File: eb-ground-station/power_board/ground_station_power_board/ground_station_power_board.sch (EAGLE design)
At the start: 70 parts, among them J1 CONN_20X2SHROUDED, Q1 SQJ459EP_MOSFET_P_CHAN, Q15 DMN61D8LVT-DUAL-N-CHANNEL-MOS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, Q17 DMN61D8LVT-DUAL-N-CHANNEL-MOS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, Q18 DMN61D8LVT-DUAL-N-CHANNEL-MOS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, Q2 SQJ459EP_MOSFET_P_CHAN, Q22 TC4427-FET-GATE-DRVR, Q23 TC4427-FET-GATE-DRVR, Q24 TC4427-FET-GATE-DRVR, Q3 SQJ459EP_MOSFET_P_CHAN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

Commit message: every time I look at this I add 40 more vias
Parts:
- added J2: (no value), SparkFun-Connectors:CONN_01PTH_NO_SILK_KIT
- added R14: 4.7k, SparkFun-Resistors:4.7KOHM-0603-1/10W-1%
- R10, R8, R9: value EXB-A10P391JC_ARRAY_EXBA-M -> 10k
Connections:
- new net N$6: J2.1, R14.1, U2.!RESET
- net 3.3V: now also R14.2
- net GND: no longer U2.!RESET
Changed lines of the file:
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@@
 <?xml version="1.0" encoding="utf-8"?>
 <!DOCTYPE eagle SYSTEM "eagle.dtd">
-<eagle version="9.1.0">
+<eagle version="9.1.1">
 <drawing>
 <settings>
@@
 <layer number="90" name="Modules" color="5" fill="1" visible="no" active="yes"/>
 <layer number="91" name="Nets" color="2" fill="1" visible="yes" active="yes"/>
-<layer number="92" name="Busses" color="1" fill="1" visible="no" active="yes"/>
+<layer number="92" name="Busses" color="1" fill="1" visible="yes" active="yes"/>
 <layer number="93" name="Pins" color="2" fill="1" visible="no" active="yes"/>
 <layer number="94" name="Symbols" color="4" fill="1" visible="yes" active="yes"/>
@@
 <part name="U1" library="GROUND-STATION-POWER-BOARD" deviceset="ADS1115IDGST" device="DGS10-M"/>
 <part name="U2" library="GROUND-STATION-POWER-BOARD" deviceset="MCP23017T-E/SO" device="QFN" value="MCP23017T-E/SOQFN"/>
-<part name="R9" library="temp-lib" deviceset="EXB-A10P391J" device="C_ARRAY_EXBA-M"/>
-<part name="R8" library="temp-lib" deviceset="EXB-A10P391J" device="C_ARRAY_EXBA-M"/>
+<part name="R9" library="temp-lib" deviceset="EXB-A10P391J" device="C_ARRAY_EXBA-M" value="10k"/>
+<part name="R8" library="temp-lib" deviceset="EXB-A10P391J" device="C_ARRAY_EXBA-M" value="10k"/>
 <part name="GND1" library="SparkFun-PowerSymbols" deviceset="GND" device=""/>
 <part name="GND2" library="SparkFun-PowerSymbols" deviceset="GND" device=""/>
@@
 <part name="R2" library="SparkFun-Resistors" deviceset="4.7KOHM" device="-0603-1/10W-1%" value="4.7k"/>
 <part name="SUPPLY20" library="SparkFun-PowerSymbols" deviceset="3.3V" device=""/>
-<part name="R10" library="temp-lib" deviceset="EXB-A10P391J" device="C_ARRAY_EXBA-M"/>
+<part name="R10" library="temp-lib" deviceset="EXB-A10P391J" device="C_ARRAY_EXBA-M" value="10k"/>
 <part name="SUPPLY21" library="SparkFun-PowerSymbols" deviceset="12V" device=""/>
 <part name="R12" library="GROUND-STATION-POWER-BOARD" deviceset="RES-ARRAY-742C083" device="" value="220"/>
@@
 <part name="Q6" library="GROUND-STATION-POWER-BOARD" deviceset="SQJ459EP_MOSFET_P_CHAN" device=""/>
 <part name="FRAME1" library="frames" library_urn="urn:adsk.eagle:library:229" deviceset="FRAME_B_L" device=""/>
+<part name="R14" library="SparkFun-Resistors" deviceset="4.7KOHM" device="-0603-1/10W-1%" value="4.7k"/>
+<part name="SUPPLY15" library="SparkFun-PowerSymbols" deviceset="3.3V" device=""/>
+<part name="J2" library="SparkFun-Connectors" deviceset="CONN_01" device="PTH_NO_SILK_KIT"/>
 </parts>
 <sheets>
@@
 <attribute name="VALUE" x="-66.3194" y="489.1786" size="1.27" layer="96" ratio="6" rot="SR0"/>
 </instance>
-<instance part="R9" gate="A" x="21.59" y="482.6" smashed="yes"/>
+<instance part="R9" gate="A" x="21.59" y="482.6" smashed="yes">
+<attribute name="VALUE" x="22.7076" y="474.5228" size="1.27" layer="96" ratio="10" rot="SR0"/>
+<attribute name="NAME" x="22.5552" y="476.5548" size="1.27" layer="95" ratio="10" rot="SR0"/>
+</instance>
 <instance part="R8" gate="A" x="21.59" y="462.28" smashed="yes">
-<attribute name="NAME" x="1.9812" y="470.7128" size="1.27" layer="95" ratio="10" rot="SR0"/>
+<attribute name="VALUE" x="22.4536" y="455.7268" size="1.27" layer="96" ratio="10" rot="SR0"/>
+<attribute name="NAME" x="22.3012" y="458.0128" size="1.27" layer="95" ratio="10" rot="SR0"/>
 </instance>
 <instance part="GND1" gate="1" x="26.67" y="467.36" smashed="yes">
@@
 <attribute name="VALUE" x="-39.37" y="336.804" size="1.27" layer="96" align="bottom-center"/>
 </instance>
-<instance part="GND7" gate="1" x="-73.66" y="447.04" smashed="yes">
-<attribute name="VALUE" x="-73.66" y="446.786" size="1.27" layer="96" align="top-center"/>
+<instance part="GND7" gate="1" x="-78.74" y="459.74" smashed="yes">
+<attribute name="VALUE" x="-78.74" y="459.486" size="1.27" layer="96" align="top-center"/>
 </instance>
 <instance part="GND8" gate="1" x="-50.8" y="424.18" smashed="yes">
@@
 </instance>
 <instance part="R10" gate="A" x="170.18" y="383.54" smashed="yes">
-<attribute name="NAME" x="172.1612" y="369.1128" size="1.27" layer="95" ratio="10" rot="SR0"/>
+<attribute name="VALUE" x="171.0436" y="369.8748" size="1.27" layer="96" ratio="10" rot="SR0"/>
+<attribute name="NAME" x="170.8912" y="371.6528" size="1.27" layer="95" ratio="10" rot="SR0"/>
 </instance>
 <instance part="SUPPLY21" gate="G$1" x="175.26" y="375.92" smashed="yes">
@@
 <instance part="FRAME1" gate="G$1" x="-93.98" y="231.14"/>
 <instance part="FRAME1" gate="G$2" x="231.14" y="231.14"/>
+<instance part="R14" gate="G$1" x="-83.82" y="457.2" smashed="yes" rot="R90">
+<attribute name="NAME" x="-85.344" y="457.2" size="1.27" layer="95" font="vector" rot="R90" align="bottom-center"/>
+<attribute name="VALUE" x="-82.296" y="457.2" size="1.27" layer="96" font="vector" rot="R90" align="top-center"/>
+</instance>
+<instance part="SUPPLY15" gate="G$1" x="-83.82" y="463.804" smashed="yes">
+<attribute name="VALUE" x="-83.82" y="466.598" size="1.27" layer="96" align="bottom-center"/>
+</instance>
+<instance part="J2" gate="G$1" x="-83.82" y="439.42" rot="R90"/>
 </instances>
 <busses>
@@
 <wire x1="26.67" y1="469.9" x2="26.67" y2="472.44" width="0.1524" layer="91"/>
 <wire x1="26.67" y1="472.44" x2="24.13" y2="472.44" width="0.1524" layer="91"/>
-</segment>
-<segment>
-<pinref part="GND7" gate="1" pin="GND"/>
-<pinref part="U2" gate="A" pin="!RESET"/>
-<wire x1="-73.66" y1="449.58" x2="-73.66" y2="452.12" width="0.1524" layer="91"/>
-<wire x1="-73.66" y1="452.12" x2="-71.12" y2="452.12" width="0.1524" layer="91"/>
-<pinref part="U2" gate="A" pin="A0"/>
-<wire x1="-71.12" y1="462.28" x2="-73.66" y2="462.28" width="0.1524" layer="91"/>
-<wire x1="-73.66" y1="462.28" x2="-73.66" y2="459.74" width="0.1524" layer="91"/>
-<junction x="-73.66" y="452.12"/>
-<pinref part="U2" gate="A" pin="A1"/>
-<wire x1="-73.66" y1="459.74" x2="-73.66" y2="457.2" width="0.1524" layer="91"/>
-<wire x1="-73.66" y1="457.2" x2="-73.66" y2="452.12" width="0.1524" layer="91"/>
-<wire x1="-71.12" y1="459.74" x2="-73.66" y2="459.74" width="0.1524" layer="91"/>
-<junction x="-73.66" y="459.74"/>
-<pinref part="U2" gate="A" pin="A2"/>
-<wire x1="-71.12" y1="457.2" x2="-73.66" y2="457.2" width="0.1524" layer="91"/>
-<junction x="-73.66" y="457.2"/>
 </segment>
 <segment>
@@
 <wire x1="-43.18" y1="297.18" x2="-43.18" y2="300.99" width="0.1524" layer="91"/>
 </segment>
+<segment>
+<pinref part="U2" gate="A" pin="A0"/>
+<wire x1="-71.12" y1="462.28" x2="-73.66" y2="462.28" width="0.1524" layer="91"/>
+<wire x1="-73.66" y1="462.28" x2="-73.66" y2="459.74" width="0.1524" layer="91"/>
+<pinref part="U2" gate="A" pin="A1"/>
+<wire x1="-73.66" y1="459.74" x2="-73.66" y2="457.2" width="0.1524" layer="91"/>
+<wire x1="-71.12" y1="459.74" x2="-73.66" y2="459.74" width="0.1524" layer="91"/>
+<junction x="-73.66" y="459.74"/>
+<pinref part="U2" gate="A" pin="A2"/>
+<wire x1="-71.12" y1="457.2" x2="-73.66" y2="457.2" width="0.1524" layer="91"/>
+<pinref part="GND7" gate="1" pin="GND"/>
+<wire x1="-78.74" y1="462.28" x2="-73.66" y2="462.28" width="0.1524" layer="91"/>
+<junction x="-73.66" y="462.28"/>
+</segment>
 </net>
 <net name="12V" class="0">
@@
 <pinref part="SUPPLY9" gate="G$1" pin="3.3V"/>
 <wire x1="-44.45" y1="334.01" x2="-39.37" y2="334.01" width="0.1524" layer="91"/>
+</segment>
+<segment>
+<pinref part="SUPPLY15" gate="G$1" pin="3.3V"/>
+<pinref part="R14" gate="G$1" pin="2"/>
+<wire x1="-83.82" y1="463.804" x2="-83.82" y2="462.28" width="0.1524" layer="91"/>
 </segment>
 </net>
@@
 </segment>
 </net>
+<net name="N$6" class="0">
+<segment>
+<pinref part="U2" gate="A" pin="!RESET"/>
+<pinref part="R14" gate="G$1" pin="1"/>
+<wire x1="-71.12" y1="452.12" x2="-83.82" y2="452.12" width="0.1524" layer="91"/>
+<pinref part="J2" gate="G$1" pin="1"/>
+<wire x1="-83.82" y1="452.12" x2="-83.82" y2="447.04" width="0.1524" layer="91"/>
+<junction x="-83.82" y="452.12"/>
+</segment>
+</net>

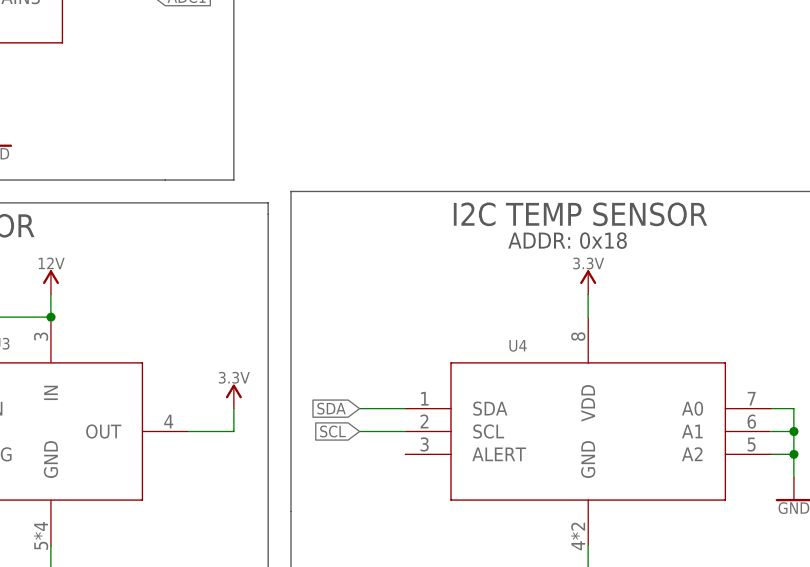
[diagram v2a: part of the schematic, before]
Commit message: added decoupling cap and some labels
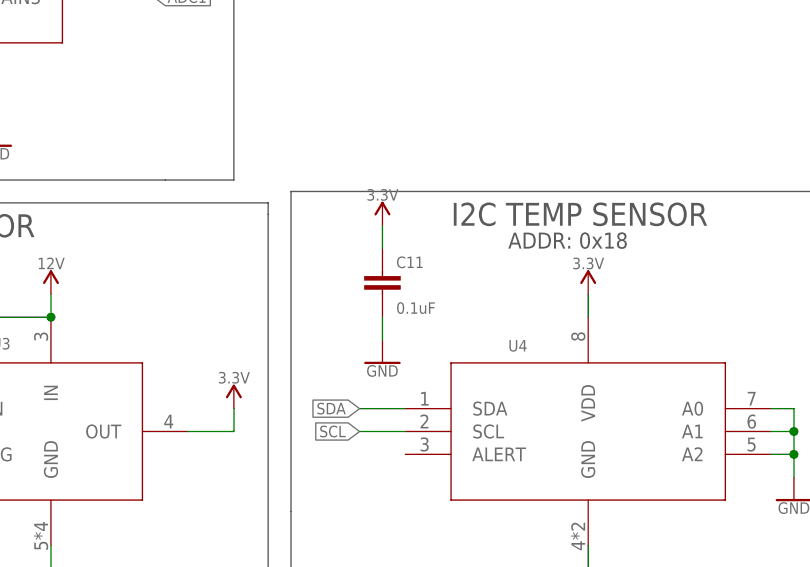
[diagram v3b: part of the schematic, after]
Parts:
- added C11: 0.1uF, SparkFun-Capacitors:0.1UF-0603-25V-5%
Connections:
- net 3.3V: now also C11.1
- net GND: now also C11.2
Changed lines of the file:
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@@
 <part name="SUPPLY15" library="SparkFun-PowerSymbols" deviceset="3.3V" device=""/>
 <part name="J2" library="SparkFun-Connectors" deviceset="CONN_01" device="PTH_NO_SILK_KIT"/>
+<part name="C11" library="SparkFun-Capacitors" deviceset="0.1UF" device="-0603-25V-5%" value="0.1uF"/>
+<part name="SUPPLY27" library="SparkFun-PowerSymbols" deviceset="3.3V" device=""/>
+<part name="GND3" library="SparkFun-PowerSymbols" deviceset="GND" device=""/>
 </parts>
 <sheets>
@@
 </instance>
 <instance part="J2" gate="G$1" x="-83.82" y="439.42" rot="R90"/>
+<instance part="C11" gate="G$1" x="0" y="278.13" smashed="yes">
+<attribute name="NAME" x="1.524" y="281.051" size="1.27" layer="95" font="vector"/>
+<attribute name="VALUE" x="1.524" y="275.971" size="1.27" layer="96" font="vector"/>
+</instance>
+<instance part="SUPPLY27" gate="G$1" x="0" y="285.75" smashed="yes">
+<attribute name="VALUE" x="0" y="288.544" size="1.27" layer="96" align="bottom-center"/>
+</instance>
+<instance part="GND3" gate="1" x="0" y="270.51" smashed="yes">
+<attribute name="VALUE" x="0" y="270.256" size="1.27" layer="96" align="top-center"/>
+</instance>
 </instances>
 <busses>
@@
 <junction x="-73.66" y="462.28"/>
 </segment>
+<segment>
+<pinref part="C11" gate="G$1" pin="2"/>
+<pinref part="GND3" gate="1" pin="GND"/>
+<wire x1="0" y1="275.59" x2="0" y2="273.05" width="0.1524" layer="91"/>
+</segment>
 </net>
 <net name="12V" class="0">
@@
 <wire x1="-83.82" y1="463.804" x2="-83.82" y2="462.28" width="0.1524" layer="91"/>
 </segment>
-</net>
+<segment>
+<pinref part="C11" gate="G$1" pin="1"/>
+<pinref part="SUPPLY27" gate="G$1" pin="3.3V"/>
+<wire x1="0" y1="283.21" x2="0" y2="285.75" width="0.1524" layer="91"/>
+</segment>
+</net>

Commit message: added SMPS
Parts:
- removed C3, C4: 10uF, SparkFun-Capacitors:10UF-0805-10V-10%
- removed C5: 0.1uF, SparkFun-Capacitors:0.1UF-0603-25V-5%
- removed U3: MIC5239-3.3YMMMSOP-8_MM-M, GROUND-STATION-POWER-BOARD:MIC5239-3.3YMMMSOP-8_MM-M
- added C12: 10uF, SparkFun-Capacitors:10UF-1206-6.3V-20%
- added C13: 22UF-1210-16V-20%, SparkFun-Capacitors:22UF-1210-16V-20%
- added TP1: TEST-POINT3, SparkFun-Connectors:TEST-POINT3
- added U$9: LMZM23601V3SILT, GROUND-STATION-POWER-BOARD:LMZM23601V3SILT
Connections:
- new net N$7: TP1.1, U$9.PGOOD
- net 12V: now also C12.1, U$9.EN, U$9.MODE, U$9.VIN; no longer C4.1, U3.EN, U3.IN
- net 3.3V: now also C13.1, U$9.FB, U$9.VOUT; no longer C3.1, C5.1, U3.OUT
- net GND: now also C12.2, C13.2, U$9.GND; no longer C3.2, C4.2, C5.2, U3.GND
